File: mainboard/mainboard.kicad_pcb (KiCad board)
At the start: 2 copper layers, 68 x 86.5 mm, 74 parts, among them J1 Servo, J2 Buzzer, J4 Button Interface, J5 Power, J6 Release Button, J7 Extra Pins, Q1 BSS138, Q2 BSS138, Q3 BSS138, Q4 BSS138, Q5 BSS138, Q6 BSS138, SW1 SW_Push, U1 RP2040, U2 W25Q128JVS, U3 RV-3028-C7, U4 ITR9608-F, U5 TCA9535RTWR, U6 LTC-4627JD, Y1 Crystal_ABM8

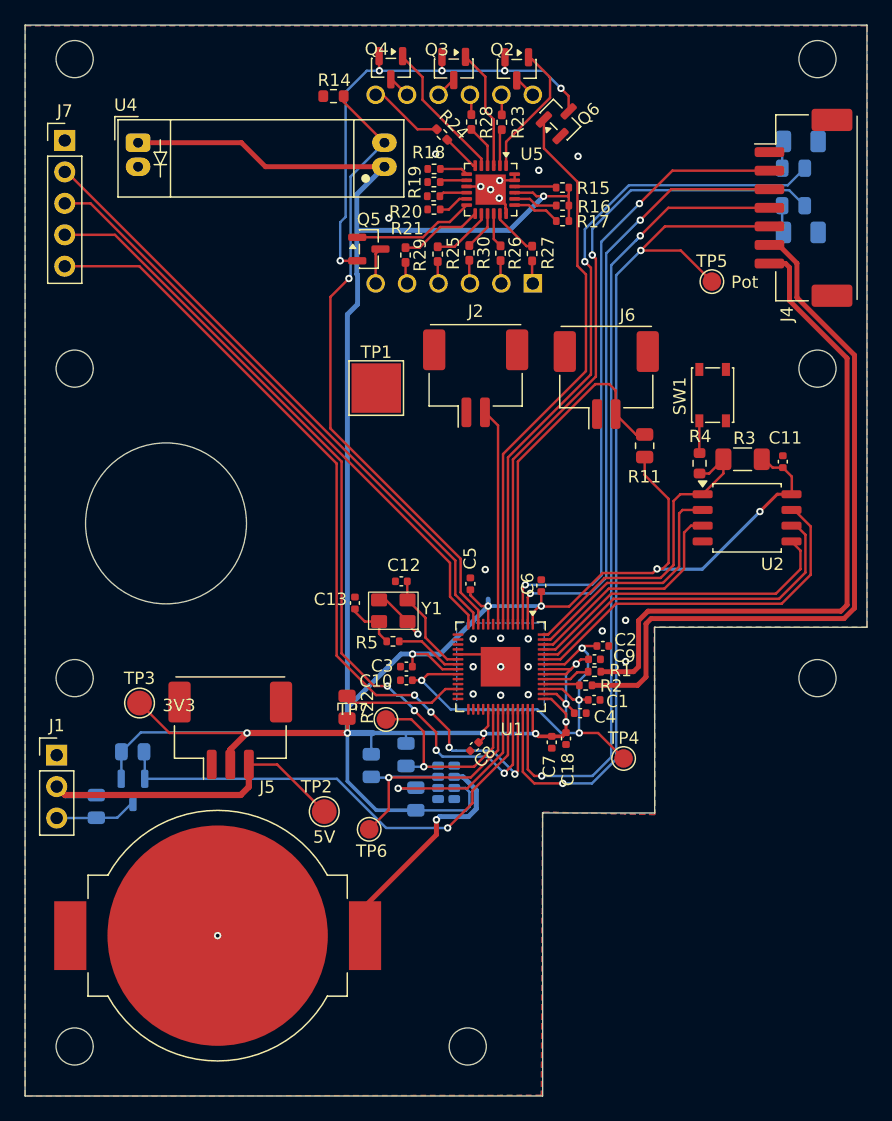
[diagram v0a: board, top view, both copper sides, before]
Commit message: Organization & rules check fixes
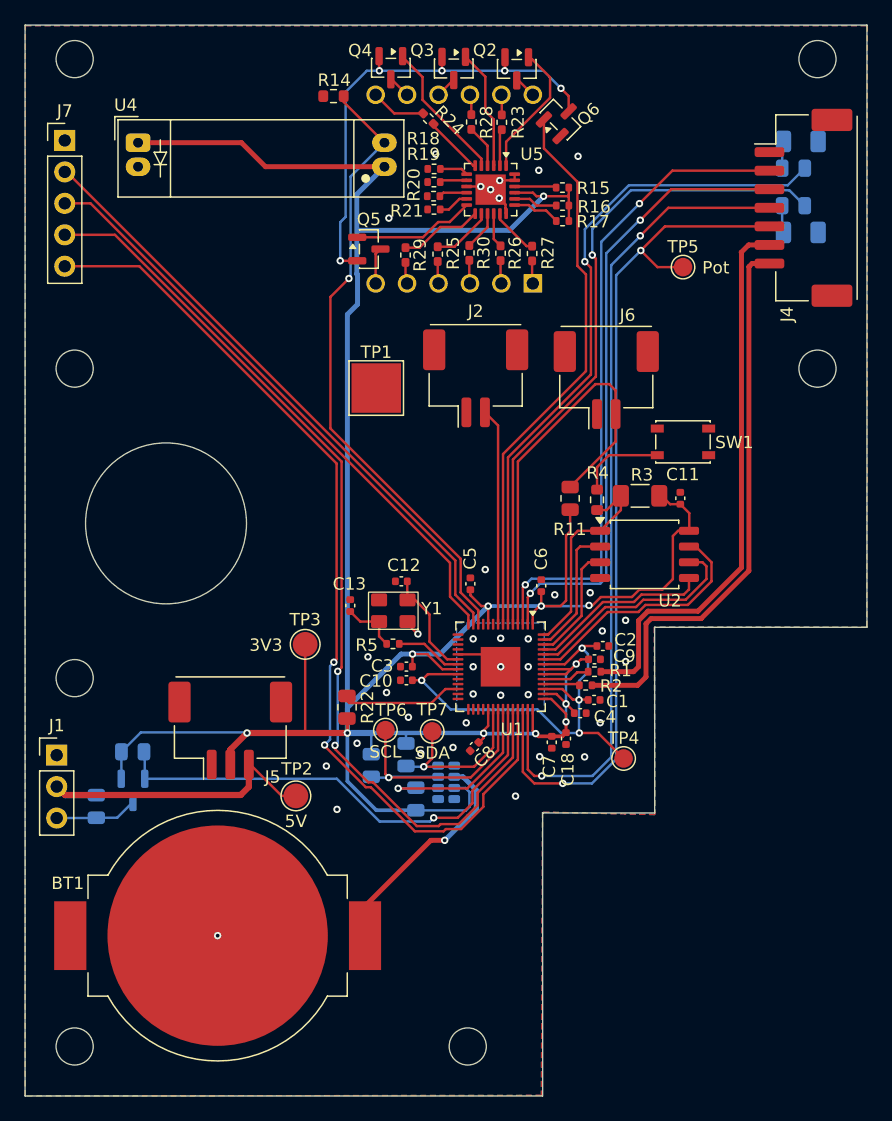
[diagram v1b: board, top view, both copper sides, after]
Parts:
- TP6: value Pot -> SCL
- TP7: value Pot -> SDA
- moved TP3 14.2 mm to (100.4, 107.5)
- moved C11 8.79 mm to (130.7, 95.7)
- moved R4 8.79 mm to (123.9, 95.8)
- moved U2 8.79 mm to (127.8, 100.3)
- moved R3 8.79 mm to (127.4, 95.5)
- moved TP6 8.12 mm to (106.8, 114.5)
- moved R11 7.37 mm to (121.8, 95.7)
- moved SW1 4.47 mm to (130.9, 91.2), turned to 180 degrees
- moved TP7 3.86 mm to (110.6, 114.5)
- moved TP2 2.62 mm to (99.6, 119.8)
- moved TP5 2.61 mm to (130.9, 77.0)
- moved R24 1.69 mm to (110.3, 65.1)
- moved C13 0.43 mm to (104.0, 104.4)
- moved R5 0.20 mm to (107.5, 107.5)
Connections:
- J4 pad 6: /USB D- -> /USB D+
- J4 pad 7: /USB D+ -> /USB D-
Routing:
- net /USB D-: track 58.9 -> 45.4 mm
- net /QSPI_SD0: track 26.0 -> 14.7 mm
- net +3.3V: track 261.4 -> 250.1 mm, vias 13 -> 12
- net /QSPI_SD3: track 30.4 -> 20.3 mm
- net /QSPI_SCLK: track 28.4 -> 18.7 mm
- net /USB D+: track 55.2 -> 45.8 mm
- net /QSPI_SS: track 26.5 -> 17.5 mm
- net /QSPI_SD1: track 19.7 -> 10.7 mm
- net /QSPI_SD2: track 18.6 -> 9.57 mm
- net /GPIO27_ADC1: track 68.6 -> 77.4 mm, vias 4 -> 2
- net /GPIO26_ADC0: track 68.9 -> 77.3 mm, vias 4 -> 2
- net Net-(R4-Pad1): track 2.75 -> 7.25 mm
- net /B_RELEASE: track 28.8 -> 33.2 mm
- net /RTC_SDA: track 18.2 -> 15.1 mm
- net +5V: track 29.1 -> 26.2 mm
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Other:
- outline, holes or cut-outs redrawn
- board text removed: "${REFERENCE}"

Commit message: Updated test points, moved mount points, & added some silkscreen stuff
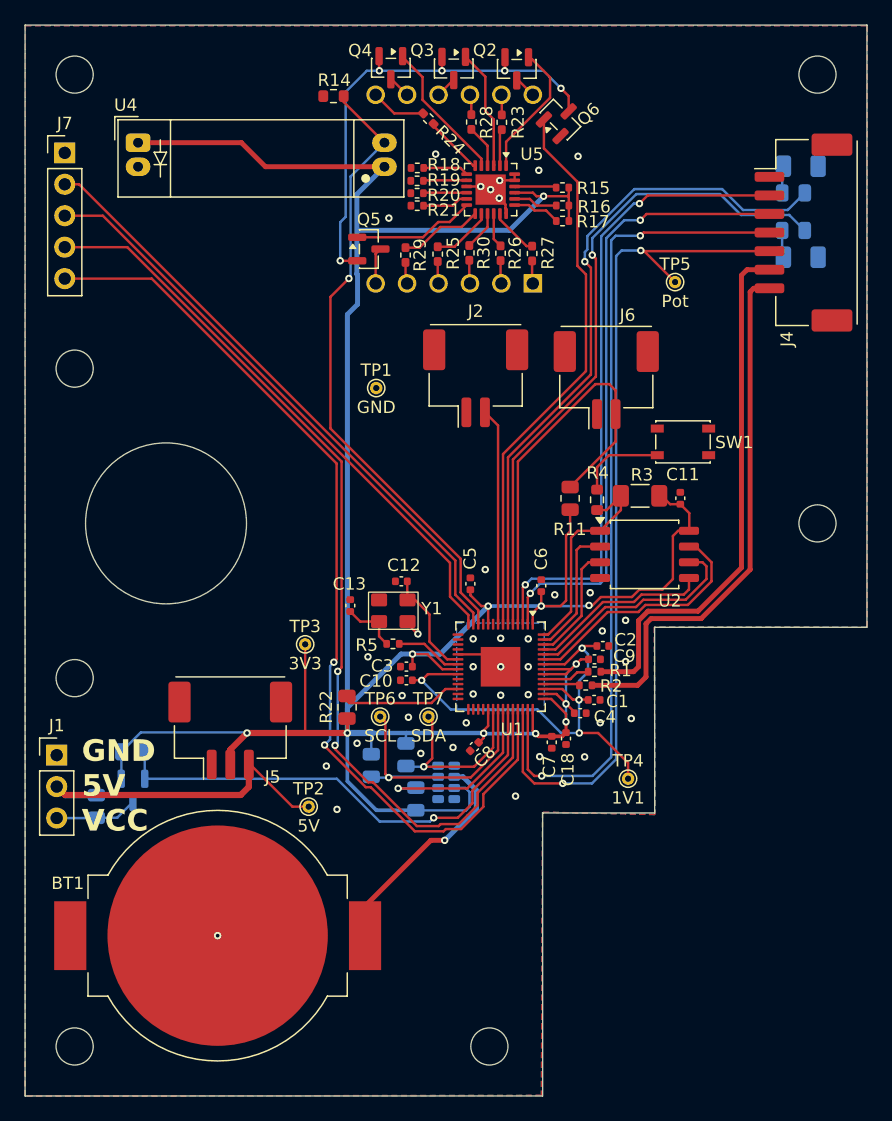
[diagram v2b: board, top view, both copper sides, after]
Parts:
- TP1: footprint TestPoint:TestPoint_Pad_4.0x4.0mm -> TestPoint:TestPoint_THTPad_D1.0mm_Drill0.5mm
- TP2, TP3: footprint TestPoint:TestPoint_Pad_D2.0mm -> TestPoint:TestPoint_THTPad_D1.0mm_Drill0.5mm
- TP4, TP5, TP6, TP7: footprint TestPoint:TestPoint_Pad_D1.5mm -> TestPoint:TestPoint_THTPad_D1.0mm_Drill0.5mm
- moved D1 2.00 mm to (140.4, 68.9)
- moved D2 2.00 mm to (140.4, 76.2)
- moved J4 2.00 mm to (140.6, 74.3)
- moved R10 2.00 mm to (139.8, 74.1)
- moved R9 2.00 mm to (139.8, 71.1)
- moved TP4 1.67 mm to (126.5, 118.4)
- moved R21 1.38 mm to (109.4, 72.1)
- moved TP5 1.37 mm to (130.2, 78.3)
- moved R19 1.36 mm to (109.4, 70.1)
- moved R18 1.35 mm to (109.4, 69.0)
- moved R20 1.35 mm to (109.4, 71.1)
- moved TP2 1.35 mm to (100.7, 120.6)
- moved TP7 1.23 mm to (110.3, 113.4)
- moved TP6 1.17 mm to (106.4, 113.4)
- moved J7 1.00 mm to (81.0, 67.8)
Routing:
- net /USB D-: track 45.4 -> 43.3 mm
- net /USB D+: track 45.8 -> 43.8 mm
- net +1V1: track 39.1 -> 40.9 mm
- net Net-(U5-P06): track 2.30 -> 3.79 mm
- net +5V: track 26.2 -> 27.6 mm
- net Net-(U5-P07): track 2.26 -> 3.58 mm
- net /RTC_SDA: track 15.1 -> 16.4 mm
- net /RTC_SCL: track 22.4 -> 23.7 mm
- net Net-(U5-P10): track 2.28 -> 3.51 mm
- net Net-(U5-P11): track 2.49 -> 3.71 mm
- net /AIN1: track 52.6 -> 52.1 mm
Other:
- outline, holes or cut-outs redrawn
- board text added: "GND 5V VCC"

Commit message: updated to 4 layer board
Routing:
- added copper zone on In1.Cu, net GND
- added copper zone on In2.Cu, net GND
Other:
- copper layers 2 -> 4
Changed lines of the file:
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@@
 	(layers
 		(0 "F.Cu" signal)
+		(4 "In1.Cu" signal)
+		(6 "In2.Cu" signal)
 		(2 "B.Cu" signal)
 		(9 "F.Adhes" user "F.Adhesive")
@@
 	)
 	(setup
+		(stackup
+			(layer "F.SilkS"
+				(type "Top Silk Screen")
+			)
+			(layer "F.Paste"
+				(type "Top Solder Paste")
+			)
+			(layer "F.Mask"
+				(type "Top Solder Mask")
+				(thickness 0.01)
+			)
+			(layer "F.Cu"
+				(type "copper")
+				(thickness 0.035)
+			)
+			(layer "dielectric 1"
+				(type "prepreg")
+				(thickness 0.1)
+				(material "FR4")
+				(epsilon_r 4.5)
+				(loss_tangent 0.02)
+			)
+			(layer "In1.Cu"
+				(type "copper")
+				(thickness 0.035)
+			)
+			(layer "dielectric 2"
+				(type "core")
+				(thickness 1.24)
+				(material "FR4")
+				(epsilon_r 4.5)
+				(loss_tangent 0.02)
+			)
+			(layer "In2.Cu"
+				(type "copper")
+				(thickness 0.035)
+			)
+			(layer "dielectric 3"
+				(type "prepreg")
+				(thickness 0.1)
+				(material "FR4")
+				(epsilon_r 4.5)
+				(loss_tangent 0.02)
+			)
+			(layer "B.Cu"
+				(type "copper")
+				(thickness 0.035)
+			)
+			(layer "B.Mask"
+				(type "Bottom Solder Mask")
+				(thickness 0.01)
+			)
+			(layer "B.Paste"
+				(type "Bottom Solder Paste")
+			)
+			(layer "B.SilkS"
+				(type "Bottom Silk Screen")
+			)
+			(copper_finish "None")
+			(dielectric_constraints no)
+		)
 		(pad_to_mask_clearance 0)
 		(allow_soldermask_bridges_in_footprints no)
@@
 		(net_name "GND")
 		(locked yes)
-		(layers "F.Cu" "B.Cu")
+		(layers "F.Cu" "B.Cu" "In1.Cu" "In2.Cu")
 		(hatch edge 0.5)
 		(priority 1)

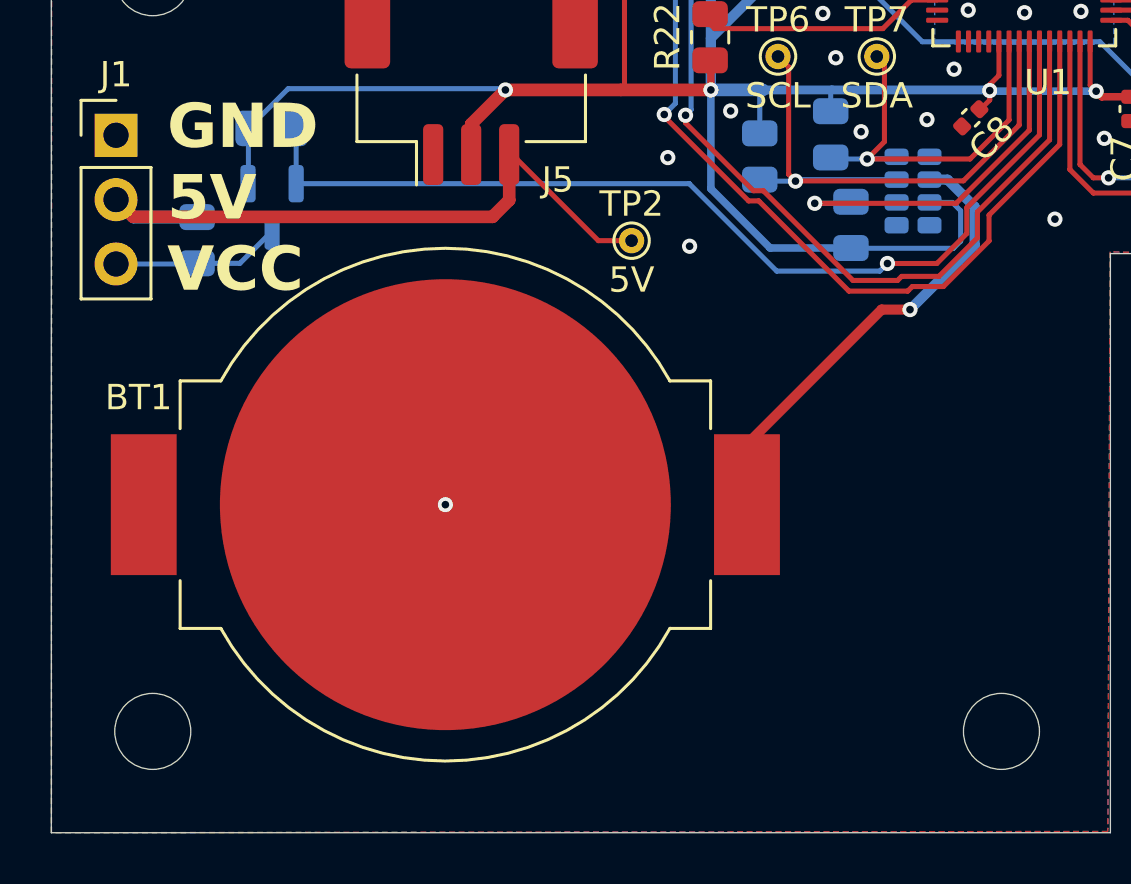
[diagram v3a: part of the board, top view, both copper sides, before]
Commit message: updated battery footprint
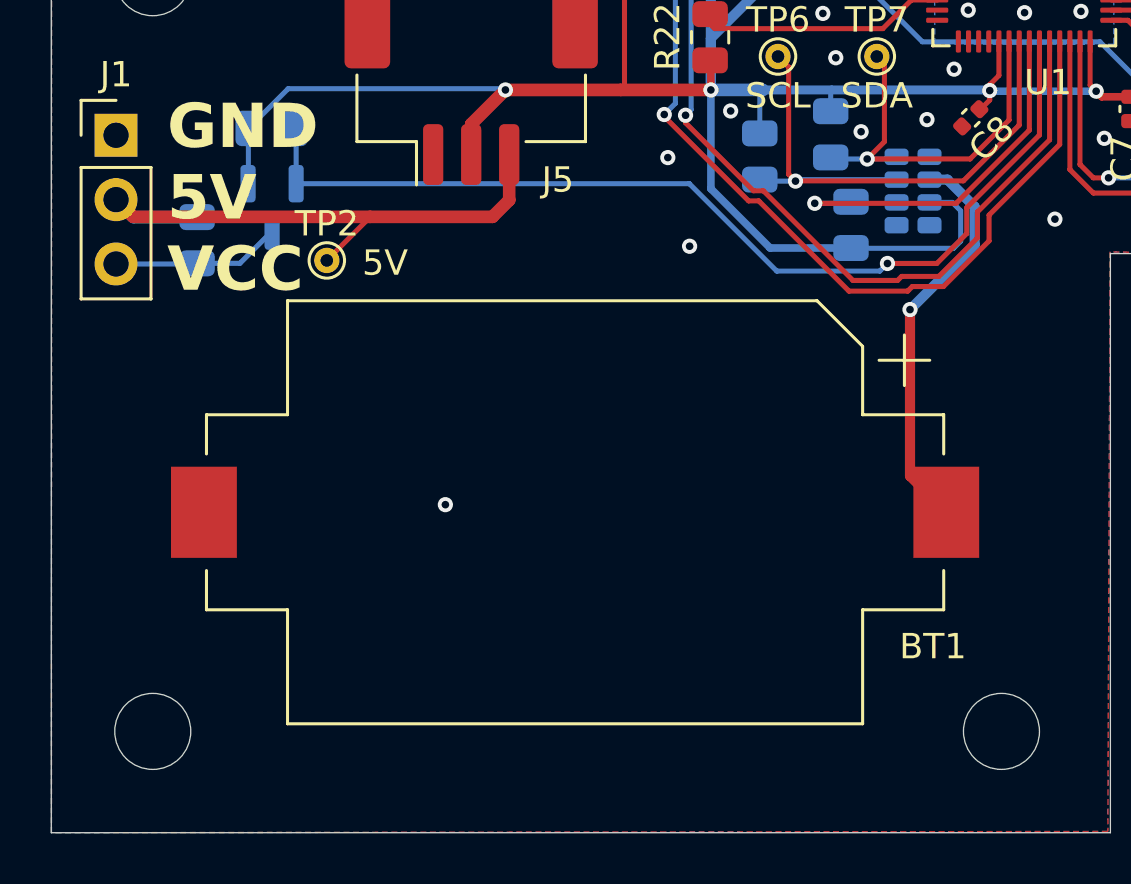
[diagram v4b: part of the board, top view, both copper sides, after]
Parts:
- BT1: footprint Battery:BatteryHolder_MPD_BC2003_1x2032 -> Battery:BatteryHolder_Keystone_1060_1x2032
- moved TP2 12.1 mm to (88.6, 121.4)
- moved BT1 5.13 mm to (98.4, 131.3), turned to 180 degrees
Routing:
- net +5V: track 27.6 -> 23.9 mm
- net Net-(BT1-+): track 18.4 -> 15.9 mm

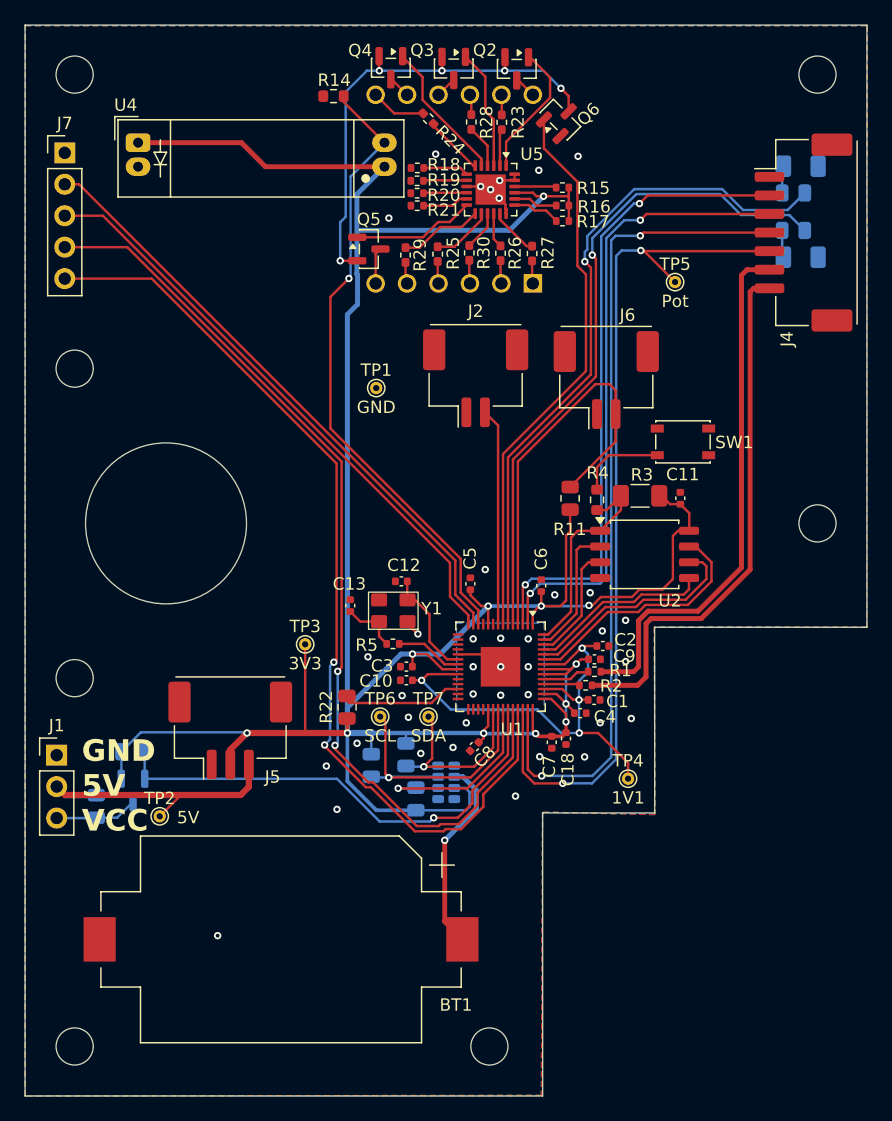
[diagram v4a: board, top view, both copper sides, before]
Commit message: switched resistors and capacitors to 0402 and updated pcb
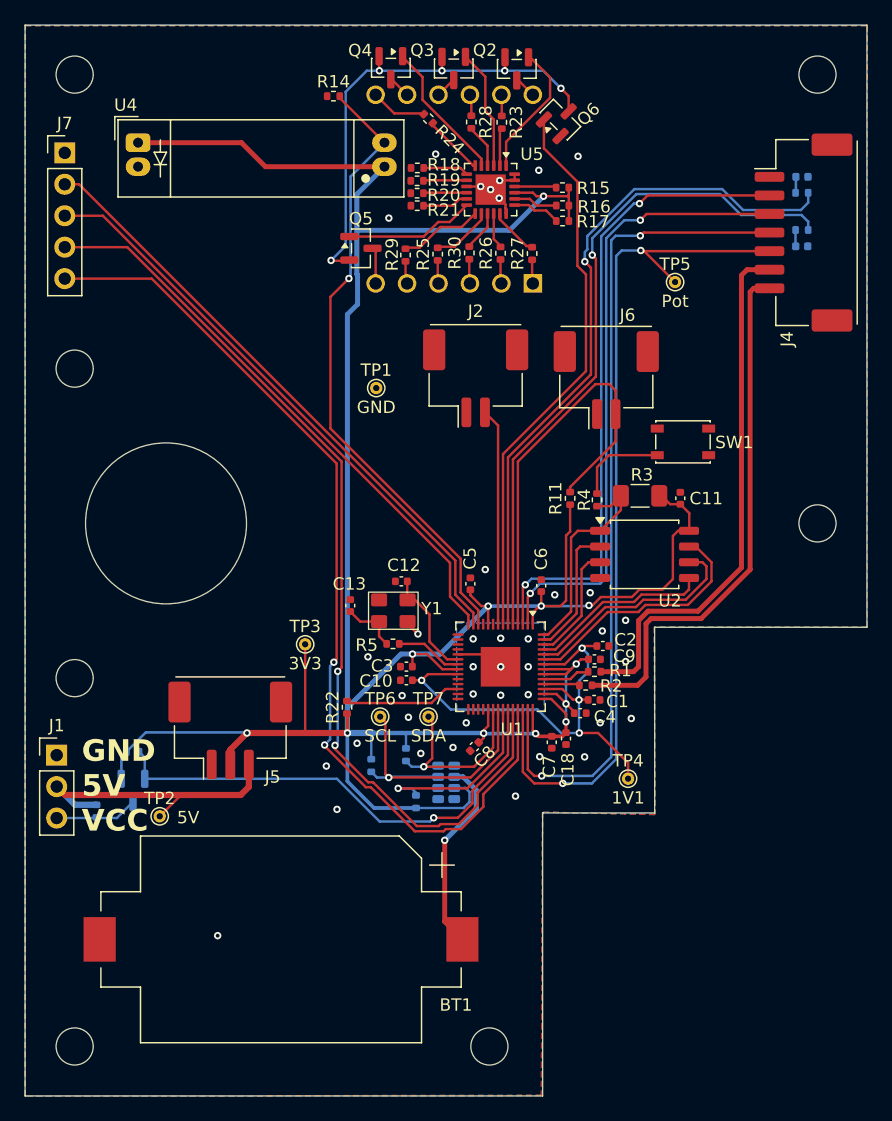
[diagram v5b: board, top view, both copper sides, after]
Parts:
- D1, D2: footprint LED_SMD:LED_1206_3216Metric -> LED_SMD:LED_0402_1005Metric
- R10, R11, R12, R13, R22, R6, R7, R8, R9: footprint Resistor_SMD:R_0805_2012Metric -> Resistor_SMD:R_0402_1005Metric
- R14, R4: footprint Resistor_SMD:R_0603_1608Metric -> Resistor_SMD:R_0402_1005Metric
- R23, R24, R25, R26, R27, R28, R29, R30: footprint Resistor_SMD:R_0402_1005Metric_Pad0.72x0.64mm_HandSolder -> Resistor_SMD:R_0402_1005Metric
- R3: value DNF -> DNF (10K)
- moved D2 0.88 mm to (140.5, 75.4)
- moved D1 0.87 mm to (140.5, 69.8)
- moved R10 0.68 mm to (140.5, 74.0)
- moved R9 0.68 mm to (140.5, 71.0)
- moved Q5 0.64 mm to (104.9, 75.5)
- moved R13 0.38 mm to (83.5, 121.0)
- moved R8 0.22 mm to (109.3, 120.2)
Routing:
- net +3.3V: track 250.1 -> 251.1 mm
- net Net-(D1-A): track 2.20 -> 1.30 mm
- net Net-(D2-A): track 2.20 -> 1.32 mm
- net /7-Segment/CC4: track 9.72 -> 10.5 mm
- net /RED_LED: track 54.0 -> 54.7 mm
- net /WHITE_LED: track 54.9 -> 55.6 mm
- net Net-(U1-RUN): track 10.0 -> 9.50 mm

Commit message: updated 7 seg
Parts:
- U6: value LTC-4627JD -> KW4-56NCWB-P-Y; footprint Display_7Segment:CA56-12SURKWA -> Display_7Segment:CC56-12GWA
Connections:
- U5 pad 11: Net-(U5-P11) -> /7-Segment/CAL
